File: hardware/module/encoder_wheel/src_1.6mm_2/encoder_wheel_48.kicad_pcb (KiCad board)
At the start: 2 copper layers, 74 x 74 mm, 2 parts

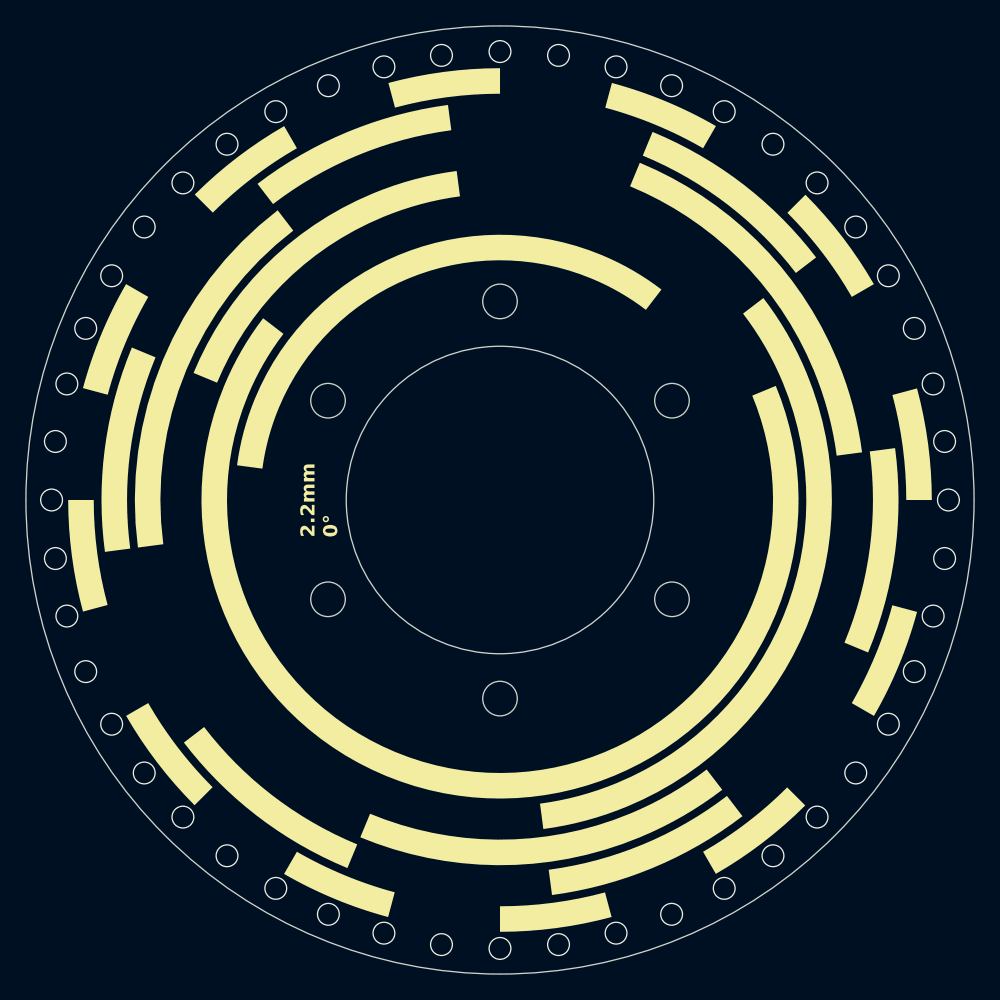
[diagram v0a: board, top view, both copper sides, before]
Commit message: add encoder wheel variants
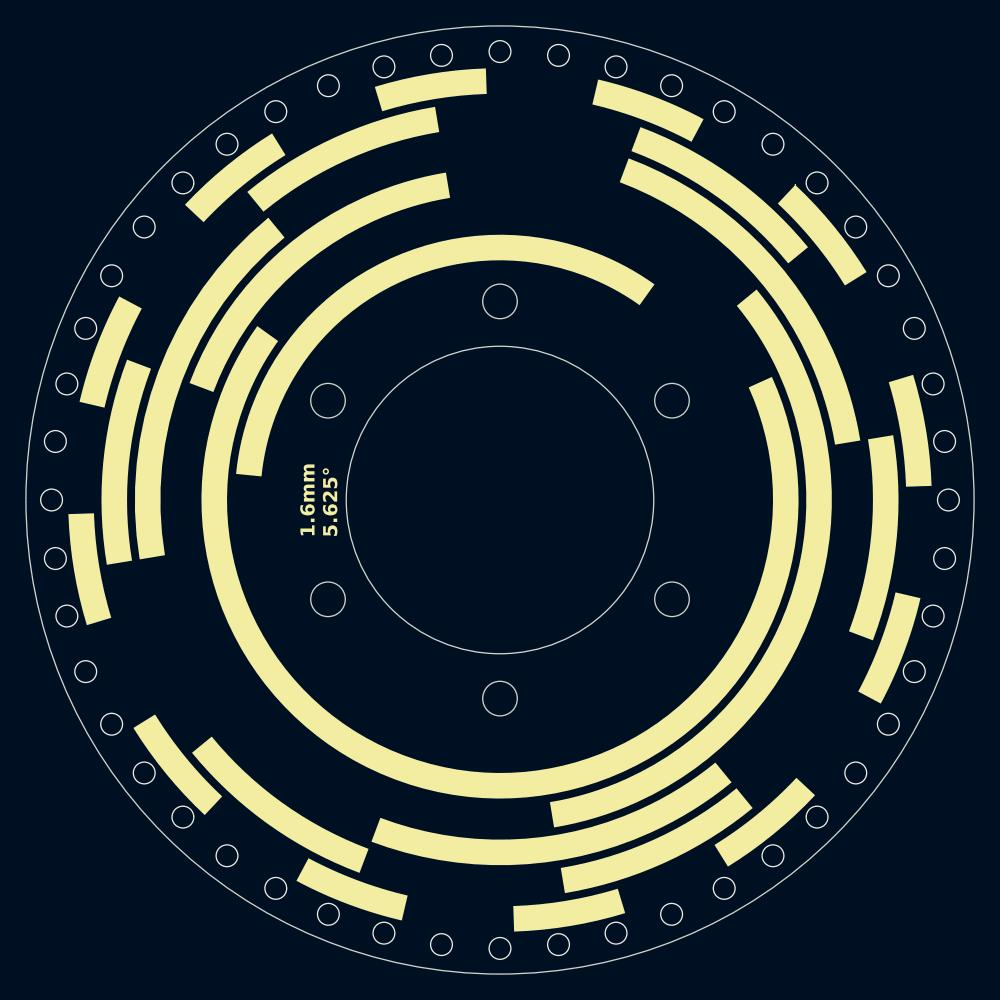
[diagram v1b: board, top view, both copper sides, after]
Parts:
- REF** (x2): value OpenFlapEncoderPattern48_2.2mm -> OpenFlapEncoderPattern48_1.6mm; footprint EncoderPattern:OpenFlapEncoderPattern48_2.2mm -> EncoderPattern:OpenFlapEncoderPattern48_1.6mm
- turned REF** to 1.875 degrees
- turned REF** to -178.125 degrees
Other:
- board text added: "1.6mm 1.875°"
- board text added: "1.6mm 5.625°"
- board text removed: "2.2mm 0°"
- board text removed: "2.2mm 3.75°"

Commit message: encoder changes
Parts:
- renumbered REF** to ENC1, REF** to ENC2

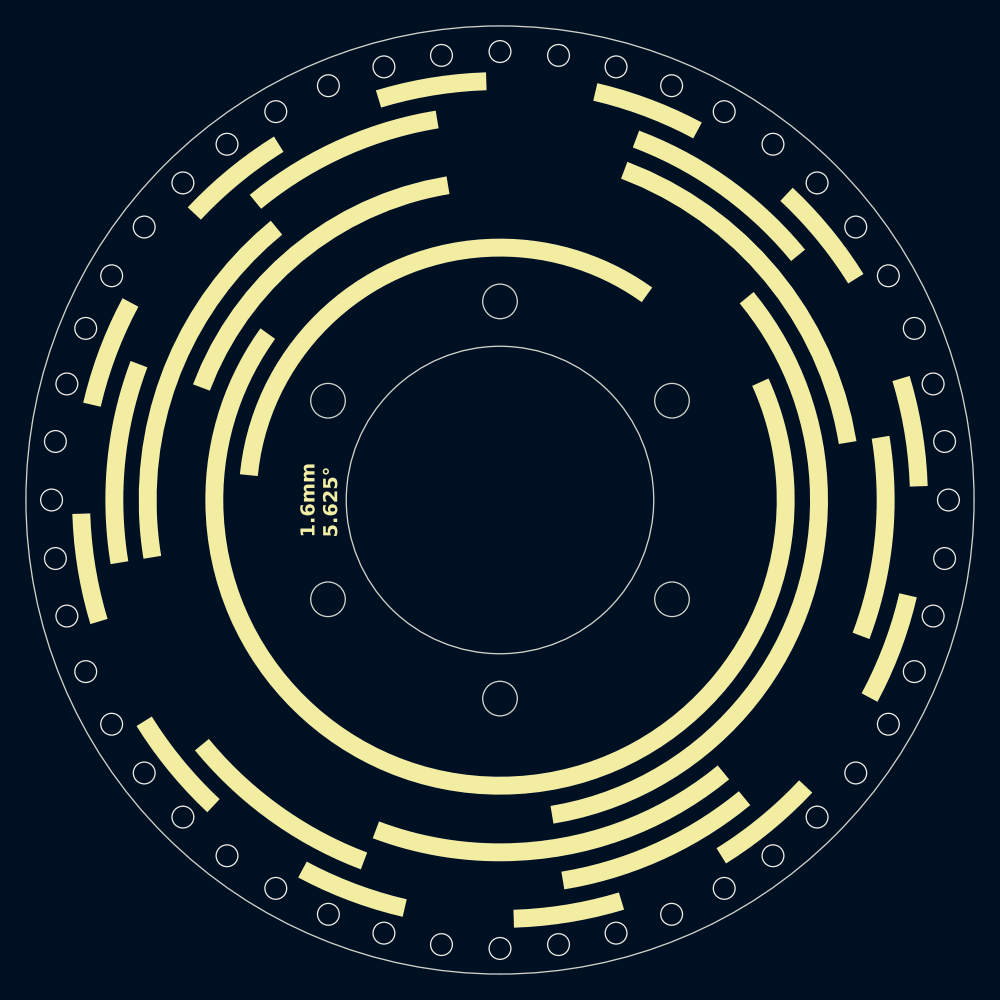
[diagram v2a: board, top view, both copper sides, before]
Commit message: changed hole patern encoder wheel
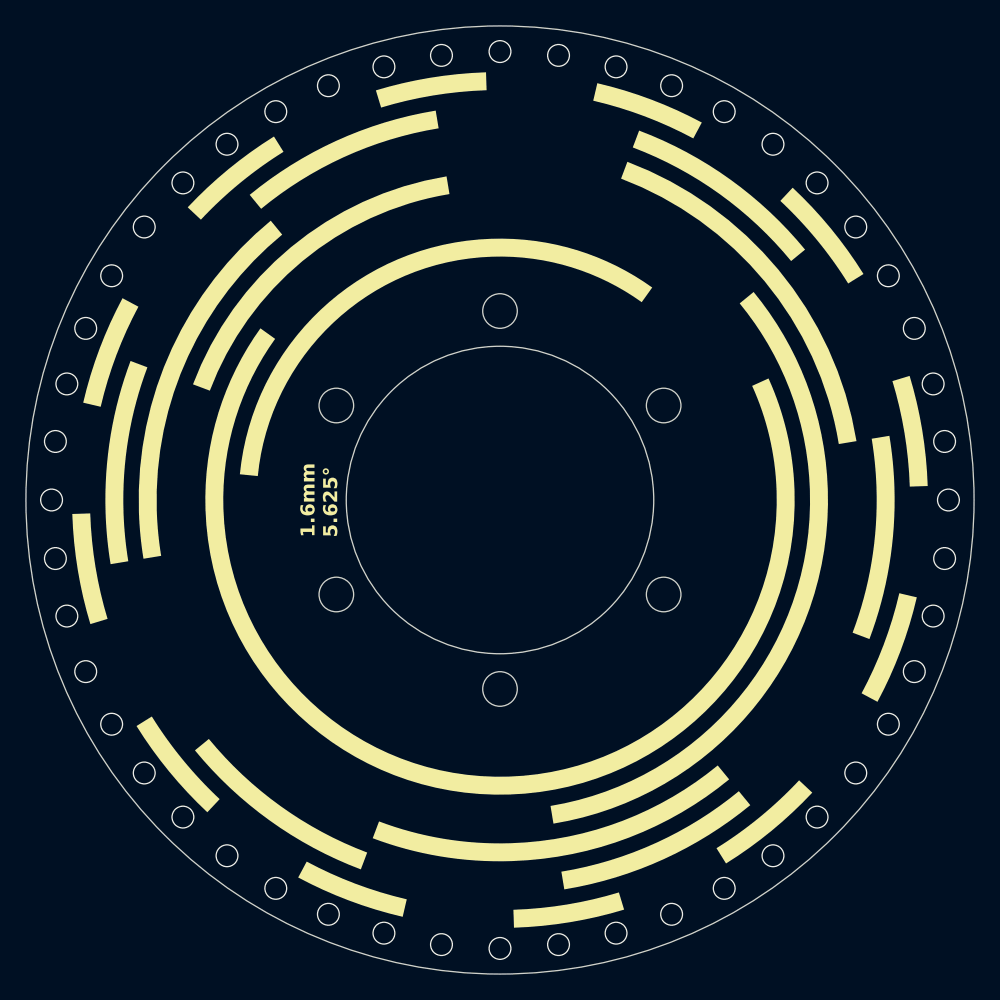
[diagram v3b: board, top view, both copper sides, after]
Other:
- outline, holes or cut-outs redrawn
